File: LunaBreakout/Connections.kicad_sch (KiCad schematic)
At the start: 4 parts, among them J1 Conn_01x02, J3 Conn_01x04, J4 Conn_01x02, U4 ISO7721D

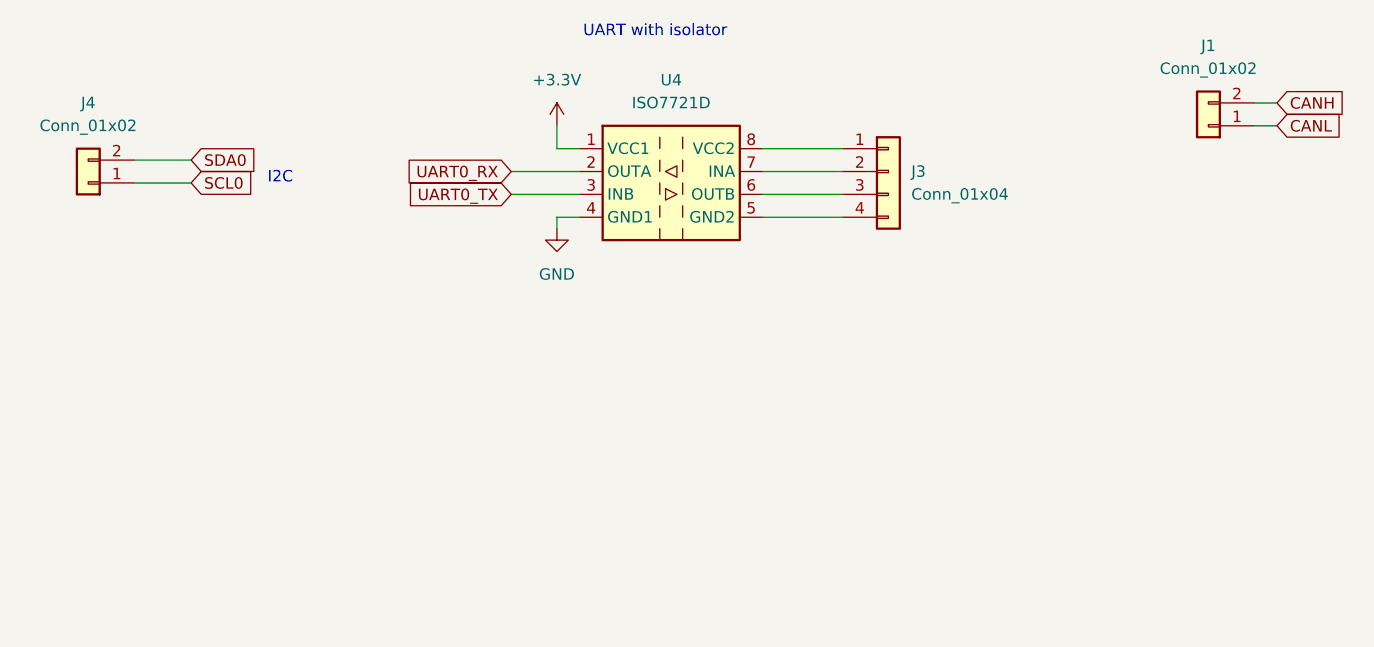
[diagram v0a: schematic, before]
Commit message: Fixed net labels, added connectors for the communication ports added
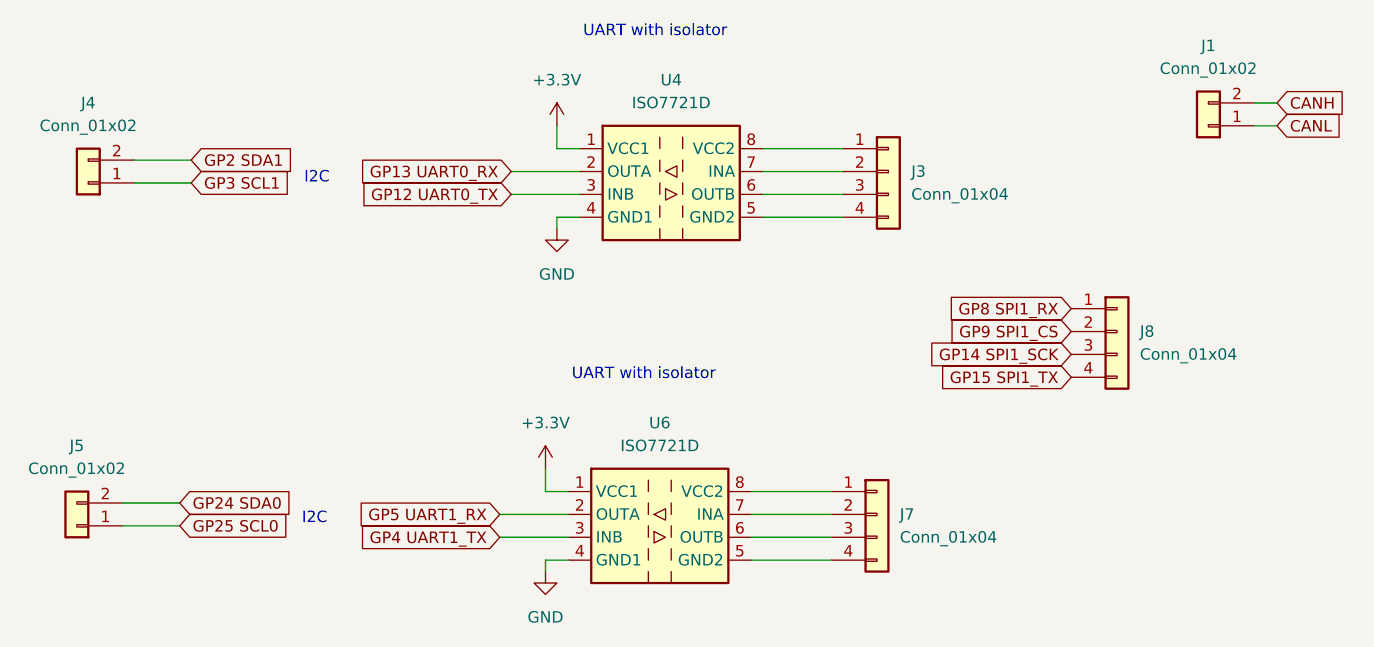
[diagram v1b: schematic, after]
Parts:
- added J5: Conn_01x02, Connector_JST:JST_XH_B2B-XH-A_1x02_P2.50mm_Vertical, symbol Connector_Generic:Conn_01x02
- added J7, J8: Conn_01x04, Connector_JST:JST_XH_B4B-XH-A_1x04_P2.50mm_Vertical, symbol Connector_Generic:Conn_01x04
- added U6: ISO7721D, Package_SO:SOIC-8_3.9x4.9mm_P1.27mm, symbol Isolator:ISO7721D
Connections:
- net +3.3V: now also U6.1 (VCC1)
- net GND: now also U6.4 (GND1)
- net SCL0 renamed GP3 SCL1
- net SDA0 renamed GP2 SDA1
- net UART0_RX renamed GP13 UART0_RX
- net UART0_TX renamed GP12 UART0_TX
- new net: J7.4 (Pin_4), U6.5 (GND2)
- new net: J7.3 (Pin_3), U6.6 (OUTB)
- new net: J7.2 (Pin_2), U6.7 (INA)
- new net: J7.1 (Pin_1), U6.8 (VCC2)
- new net GP14 SPI1_SCK: J8.3 (Pin_3)
- new net GP15 SPI1_TX: J8.4 (Pin_4)
- new net GP24 SDA0: J5.2 (Pin_2)
- new net GP25 SCL0: J5.1 (Pin_1)
- new net GP4 UART1_TX: U6.3 (INB)
- new net GP5 UART1_RX: U6.2 (OUTA)
- new net GP8 SPI1_RX: J8.1 (Pin_1)
- new net GP9 SPI1_CS: J8.2 (Pin_2)

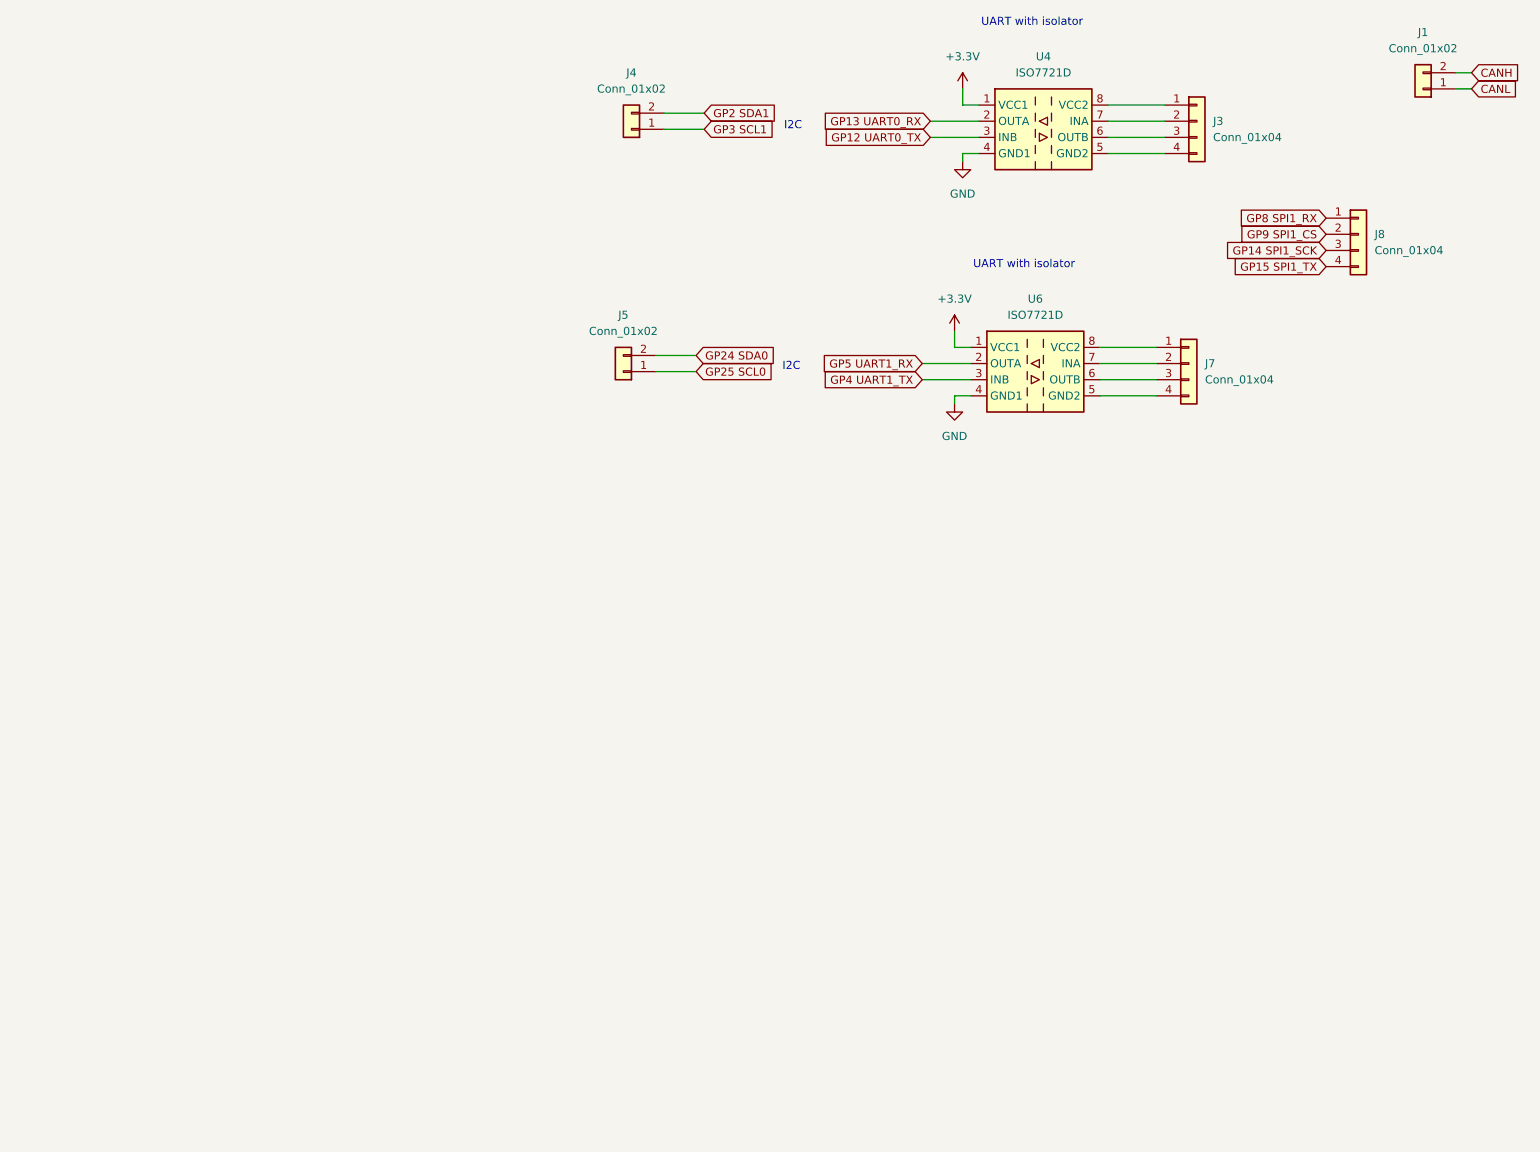
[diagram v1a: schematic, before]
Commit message: Took CAN out of schematic, changes connectorst, added misc connectors and external power symbol
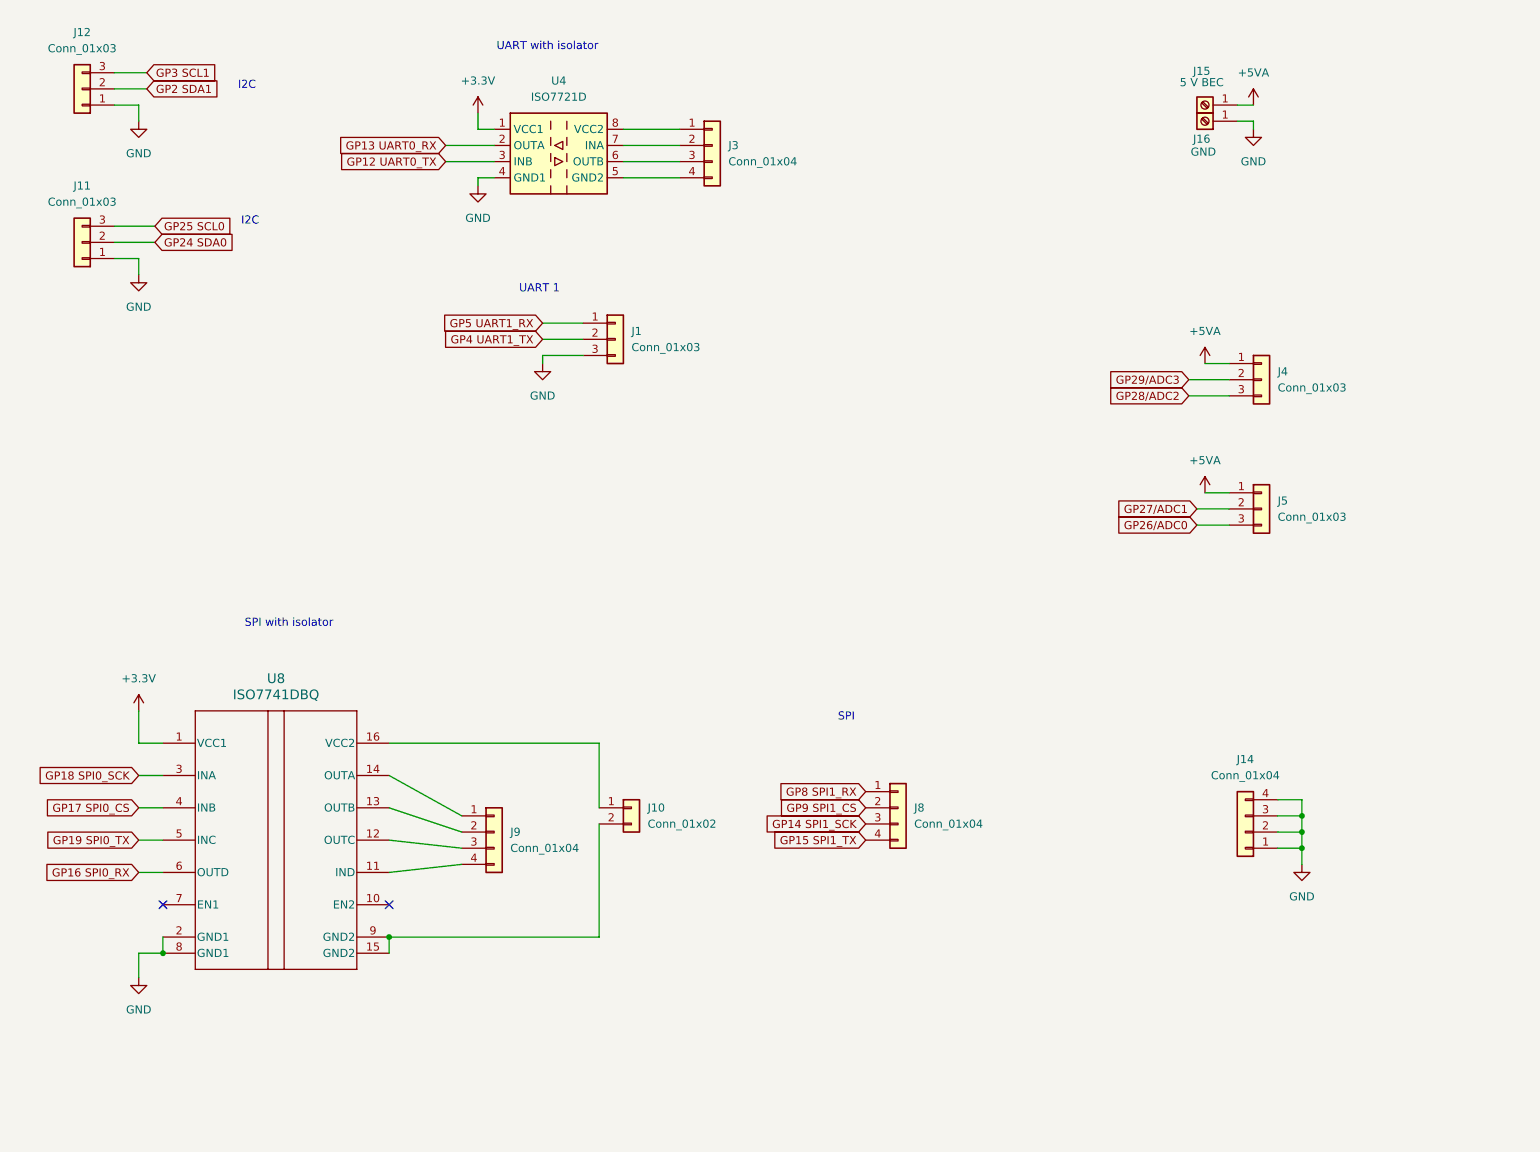
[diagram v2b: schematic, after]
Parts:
- removed J1, J4, J5: Conn_01x02, Connector_JST:JST_XH_B2B-XH-A_1x02_P2.50mm_Vertical, symbol Connector_Generic:Conn_01x02
- removed J7: Conn_01x04, Connector_JST:JST_XH_B4B-XH-A_1x04_P2.50mm_Vertical, symbol Connector_Generic:Conn_01x04
- removed U6: ISO7721D, Package_SO:SOIC-8_3.9x4.9mm_P1.27mm, symbol Isolator:ISO7721D
- added J1, J11, J12, J4, J5: Conn_01x03, Connector_JST:JST_XH_B3B-XH-A_1x03_P2.50mm_Vertical, symbol Connector_Generic:Conn_01x03
- added J10: Conn_01x02, Connector_JST:JST_XH_B2B-XH-A_1x02_P2.50mm_Vertical, symbol Connector_Generic:Conn_01x02
- added J14, J9: Conn_01x04, Connector_JST:JST_XH_B4B-XH-A_1x04_P2.50mm_Vertical, symbol Connector_Generic:Conn_01x04
- added J15: 5 V BEC, Custom_Footprints:Amphenol_Anytek_AMT0440008DB0000G, symbol Connector:Screw_Terminal_01x01
- added J16: GND, Custom_Footprints:Amphenol_Anytek_AMT0440008DB0000G, symbol Connector:Screw_Terminal_01x01
- added U8: ISO7741DBQ, ISO7741:DBQ0016A_N, symbol ISO7741:ISO7741DBQ
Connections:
- net +3.3V: now also U8.1 (VCC1)
- net GND: now also J1.3 (Pin_3), J11.1 (Pin_1), J12.1 (Pin_1), J14.1 (Pin_1), J14.2 (Pin_2), J14.3 (Pin_3), J14.4 (Pin_4), J16.1 (Pin_1), U8.2 (GND1), U8.8 (GND1)
- net GP2 SDA1: now also J12.2 (Pin_2)
- net GP24 SDA0: now also J11.2 (Pin_2)
- net GP25 SCL0: now also J11.3 (Pin_3)
- net GP3 SCL1: now also J12.3 (Pin_3)
- net GP4 UART1_TX: now also J1.2 (Pin_2)
- net GP5 UART1_RX: now also J1.1 (Pin_1)
- new net: J9.4 (Pin_4), U8.11 (IND)
- new net: J9.3 (Pin_3), U8.12 (OUTC)
- new net: J9.2 (Pin_2), U8.13 (OUTB)
- new net: J9.1 (Pin_1), U8.14 (OUTA)
- new net: J10.2 (Pin_2), U8.15 (GND2), U8.9 (GND2)
- new net: J10.1 (Pin_1), U8.16 (VCC2)
- new net +5VA: J15.1 (Pin_1), J4.1 (Pin_1), J5.1 (Pin_1)
- new net GP16 SPI0_RX: U8.6 (OUTD)
- new net GP17 SPI0_CS: U8.4 (INB)
- new net GP18 SPI0_SCK: U8.3 (INA)
- new net GP19 SPI0_TX: U8.5 (INC)
- new net GP26/ADC0: J5.3 (Pin_3)
- new net GP27/ADC1: J5.2 (Pin_2)
- new net GP28/ADC2: J4.3 (Pin_3)
- new net GP29/ADC3: J4.2 (Pin_2)
- no-connect marks 0 -> 2
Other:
- note added: "SPI"
- note added: "SPI with isolator"
- note added: "UART 1"
- moved on the sheet: J3, J8, U4

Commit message: Started on layout and traces
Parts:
- added J13, J17, J18, J19: Conn_01x04, Connector_JST:JST_XH_B4B-XH-A_1x04_P2.50mm_Vertical, symbol Connector_Generic:Conn_01x04
- added U5: ISO7720D, Package_SO:SOIC-8_3.9x4.9mm_P1.27mm, symbol Isolator:ISO7720D
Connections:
- net +3.3V: now also U5.1 (VCC1)
- net GND: now also U5.4 (GND1)
- net GP14 SPI1_SCK: now also J17.3 (Pin_3), J19.3 (Pin_3)
- net GP15 SPI1_TX: now also J17.4 (Pin_4), J19.4 (Pin_4)
- net GP8 SPI1_RX: now also J17.1 (Pin_1), J19.1 (Pin_1)
- net at J9.4 (Pin_4), U8.11 (IND): now also J13.4 (Pin_4), J18.4 (Pin_4)
- net at J9.3 (Pin_3), U8.12 (OUTC): now also J13.3 (Pin_3), J18.3 (Pin_3)
- net at J9.1 (Pin_1), U8.14 (OUTA): now also J13.1 (Pin_1), J18.1 (Pin_1)
- net at J10.2 (Pin_2), U8.15 (GND2), U8.9 (GND2): now also U5.5 (GND2)
- net at J10.1 (Pin_1), U8.16 (VCC2): now also U5.8 (VCC2)
- new net: J13.2 (Pin_2), U5.7 (OUTA)
- new net: J18.2 (Pin_2), U5.6 (OUTB)
- new net GP20: J19.2 (Pin_2)
- new net GP21: J17.2 (Pin_2)
- new net GP22: U5.3 (INB)
- new net GP23: U5.2 (INA)
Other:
- moved on the sheet: J8, J9

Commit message: Added io
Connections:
- net GND: now also J10.2 (Pin_2), J3.4 (Pin_4), U4.5 (GND2), U5.5 (GND2), U8.15 (GND2), U8.9 (GND2)
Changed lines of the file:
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@@
 	)
 	(junction
+		(at 85.09 186.69)
+		(diameter 0)
+		(color 0 0 0 0)
+	)
+	(junction
 		(at 101.6 186.69)
 		(diameter 0)
@@
 	)
 	(junction
+		(at 113.03 52.07)
+		(diameter 0)
+		(color 0 0 0 0)
+	)
+	(junction
 		(at 147.32 146.05)
 		(diameter 0)
@@
 	(wire
 		(pts
+			(xy 113.03 53.34) (xy 113.03 52.07)
+		)
+		(stroke
+			(width 0)
+			(type default)
+		)
+	)
+	(wire
+		(pts
 			(xy 199.39 96.52) (xy 204.47 96.52)
 		)
@@
 	(wire
 		(pts
-			(xy 69.85 186.69) (xy 101.6 186.69)
+			(xy 69.85 186.69) (xy 85.09 186.69)
 		)
 		(stroke
@@
 	(wire
 		(pts
+			(xy 85.09 187.96) (xy 85.09 186.69)
+		)
+		(stroke
+			(width 0)
+			(type default)
+		)
+	)
+	(wire
+		(pts
 			(xy 72.39 166.37) (xy 72.39 163.83)
 		)
@@
 	(wire
 		(pts
+			(xy 85.09 186.69) (xy 101.6 186.69)
+		)
+		(stroke
+			(width 0)
+			(type default)
+		)
+	)
+	(wire
+		(pts
 			(xy 81.28 39.37) (xy 88.9 39.37)
 		)
@@
 	)
 	(symbol
+		(lib_id "power:GND")
+		(at 113.03 53.34 0)
+		(unit 1)
+		(body_style 1)
+		(exclude_from_sim no)
+		(in_bom yes)
+		(on_board yes)
+		(in_pos_files yes)
+		(dnp no)
+		(fields_autoplaced yes)
+		(property "Reference" "#PWR043"
+			(at 113.03 59.69 0)
+			(hide yes)
+			(show_name no)
+			(do_not_autoplace no)
+			(effects
+				(font
+					(size 1.27 1.27)
+				)
+			)
+		)
+		(property "Value" "GND"
+			(at 113.03 58.42 0)
+			(show_name no)
+			(do_not_autoplace no)
+			(effects
+				(font
+					(size 1.27 1.27)
+				)
+			)
+		)
+		(property "Footprint" ""
+			(at 113.03 53.34 0)
+			(hide yes)
+			(show_name no)
+			(do_not_autoplace no)
+			(effects
+				(font
+					(size 1.27 1.27)
+				)
+			)
+		)
+		(property "Datasheet" ""
+			(at 113.03 53.34 0)
+			(hide yes)
+			(show_name no)
+			(do_not_autoplace no)
+			(effects
+				(font
+					(size 1.27 1.27)
+				)
+			)
+		)
+		(property "Description" "Power symbol creates a global label with name \"GND\" , ground"
+			(at 113.03 53.34 0)
+			(hide yes)
+			(show_name no)
+			(do_not_autoplace no)
+			(effects
+				(font
+					(size 1.27 1.27)
+				)
+			)
+		)
+		(pin "1"
+		)
+		(instances
+			(project "LunaBreakout"
+				(path "/5f8915c9-c09e-4522-819d-9a09dec9e693/10b6e54a-04b5-47c9-80e8-c4366fa1ad6e"
+					(reference "#PWR043")
+					(unit 1)
+				)
+			)
+		)
+	)
+	(symbol
 		(lib_id "power:PWR_FLAG")
 		(at 113.03 36.83 0)
@@
 					(unit 1)
 				)
+			)
+		)
+	)
+	(symbol
+		(lib_id "power:GND")
+		(at 85.09 187.96 0)
+		(unit 1)
+		(body_style 1)
+		(exclude_from_sim no)
+		(in_bom yes)
+		(on_board yes)
+		(in_pos_files yes)
+		(dnp no)
+		(fields_autoplaced yes)
+		(property "Reference" "#PWR036"
+			(at 85.09 194.31 0)
+			(hide yes)
+			(show_name no)
+			(do_not_autoplace no)
+			(effects
+				(font
+					(size 1.27 1.27)
+				)
+			)
+		)
+		(property "Value" "GND"
+			(at 85.09 193.04 0)
+			(show_name no)
+			(do_not_autoplace no)
+			(effects
+				(font
+					(size 1.27 1.27)
+				)
+			)
+		)
+		(property "Footprint" ""
+			(at 85.09 187.96 0)
+			(hide yes)
+			(show_name no)
+			(do_not_autoplace no)
+			(effects
+				(font
+					(size 1.27 1.27)
+				)
+			)
+		)
+		(property "Datasheet" ""
+			(at 85.09 187.96 0)
+			(hide yes)
+			(show_name no)
+			(do_not_autoplace no)
+			(effects
+				(font
+					(size 1.27 1.27)
+				)
+			)
+		)
+		(property "Description" "Power symbol creates a global label with name \"GND\" , ground"
+			(at 85.09 187.96 0)
+			(hide yes)
+			(show_name no)
+			(do_not_autoplace no)
+			(effects
+				(font
+					(size 1.27 1.27)
+				)
+			)
+		)
+		(pin "1"
+		)
+		(instances
+			(project "LunaBreakout"
+				(path "/5f8915c9-c09e-4522-819d-9a09dec9e693/10b6e54a-04b5-47c9-80e8-c4366fa1ad6e"
+					(reference "#PWR036")
+					(unit 1)
+				)
